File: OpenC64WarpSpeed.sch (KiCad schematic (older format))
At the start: 19 parts, among them P1 C64-Exp-Port, SW1 SW_C64_C128, SW2 SW_RESET, SW3 SW_ROM, U1 74LS109, U2 27512

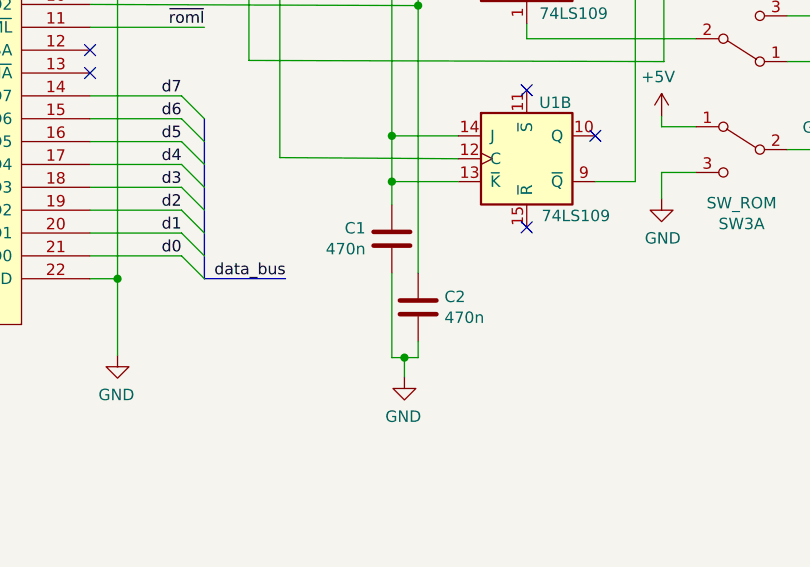
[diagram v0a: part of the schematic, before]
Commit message: Fix capacitor value: 470nF -> 47pF - Thanks @svenpetersen1965
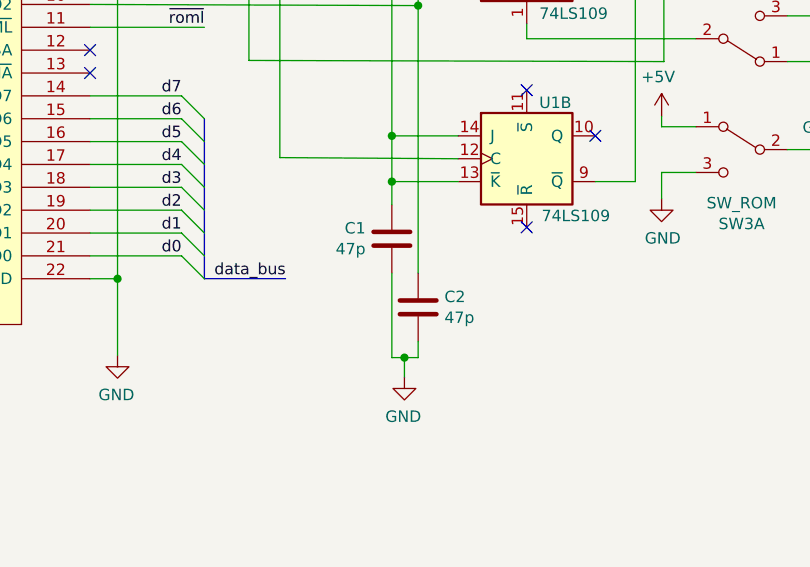
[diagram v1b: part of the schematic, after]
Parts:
- C1, C2: value 470n -> 47p
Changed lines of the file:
@@
 P 5165 4800
 F 0 "C1" H 5050 4846 50  0000 R CNN
-F 1 "470n" H 5050 4755 50  0000 R CNN
+F 1 "47p" H 5050 4755 50  0000 R CNN
 F 2 "Capacitor_THT:C_Disc_D7.5mm_W2.5mm_P5.00mm" H 5203 4650 50  0001 C CNN
 F 3 "~" H 5165 4800 50  0001 C CNN
@@
 P 5280 5100
 F 0 "C2" H 5395 5146 50  0000 L CNN
-F 1 "470n" H 5395 5055 50  0000 L CNN
+F 1 "47p" H 5395 5055 50  0000 L CNN
 F 2 "Capacitor_THT:C_Disc_D7.5mm_W2.5mm_P5.00mm" H 5318 4950 50  0001 C CNN
 F 3 "~" H 5280 5100 50  0001 C CNN
@@
 $EndComp
 $Comp
-L Graphic:Logo_Open_Hardware_Small #LOGO?
+L Graphic:Logo_Open_Hardware_Small #LOGO1
 U 1 1 5E833734
 P 10925 6870
-F 0 "#LOGO?" H 10925 7145 50  0001 C CNN
+F 0 "#LOGO1" H 10925 7145 50  0001 C CNN
 F 1 "Logo_Open_Hardware_Small" H 10925 6645 50  0001 C CNN
 F 2 "" H 10925 6870 50  0001 C CNN
